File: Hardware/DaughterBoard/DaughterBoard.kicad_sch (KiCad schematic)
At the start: 19 parts, among them J1 CARTDRIGE, J10 JOYPAD2, J11 LCD, J12 POWER, J13 PA, J14 PB, J2 ROM, J3 ISA00, J4 ISA10, J7 ISA01, J8 ISA11, J9 JOYPAD1, X1 ACO-20MHz

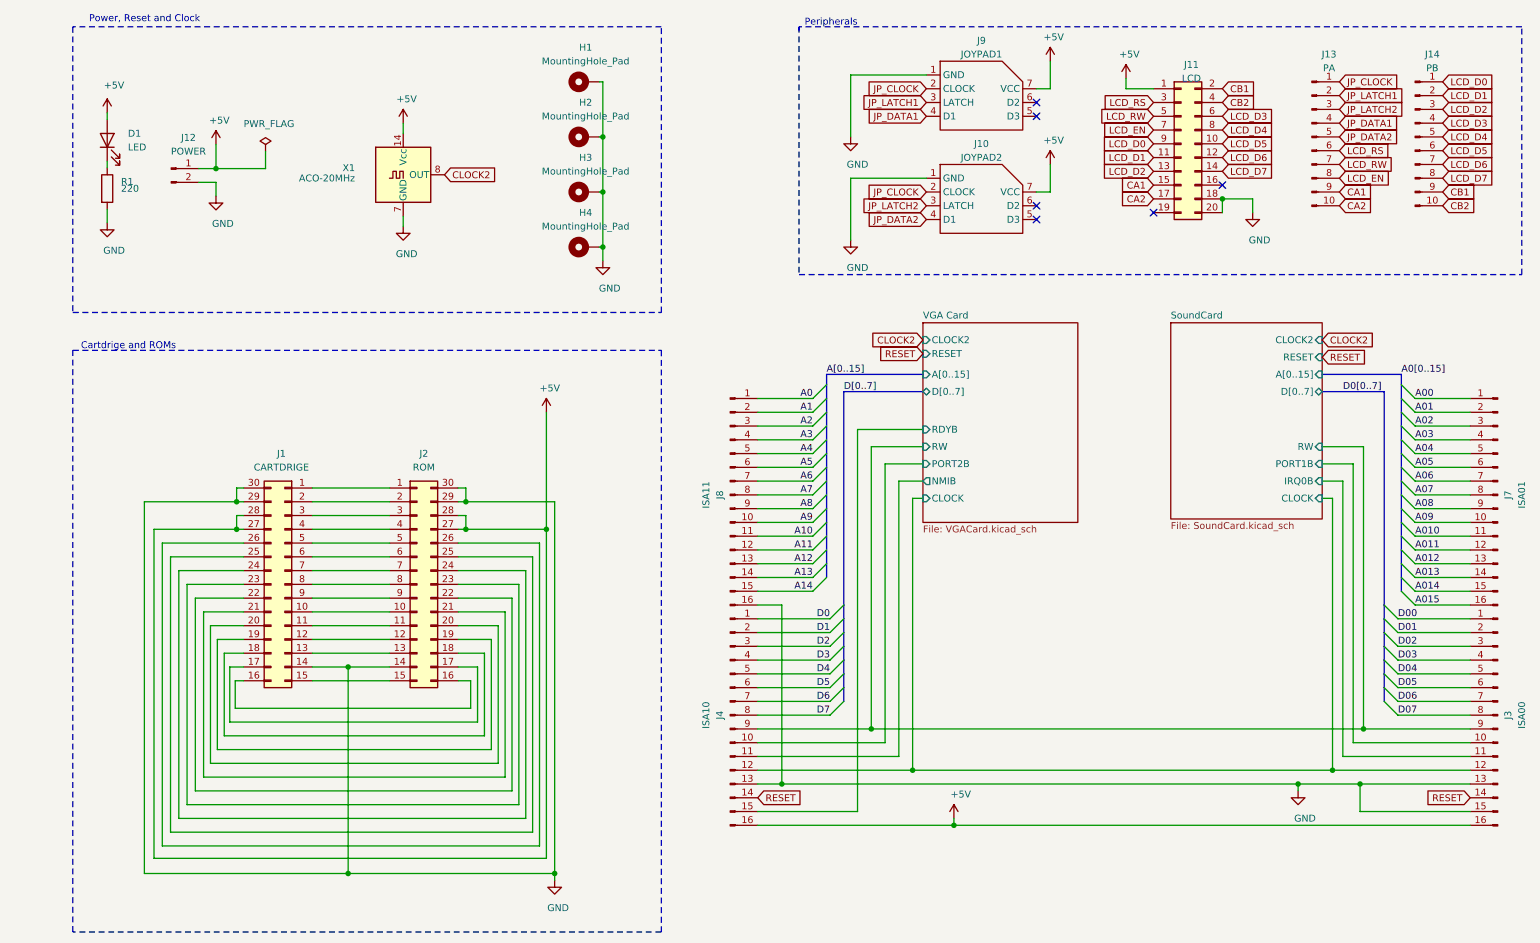
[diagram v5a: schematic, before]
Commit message: New PLD logic, VGA, DMA ...
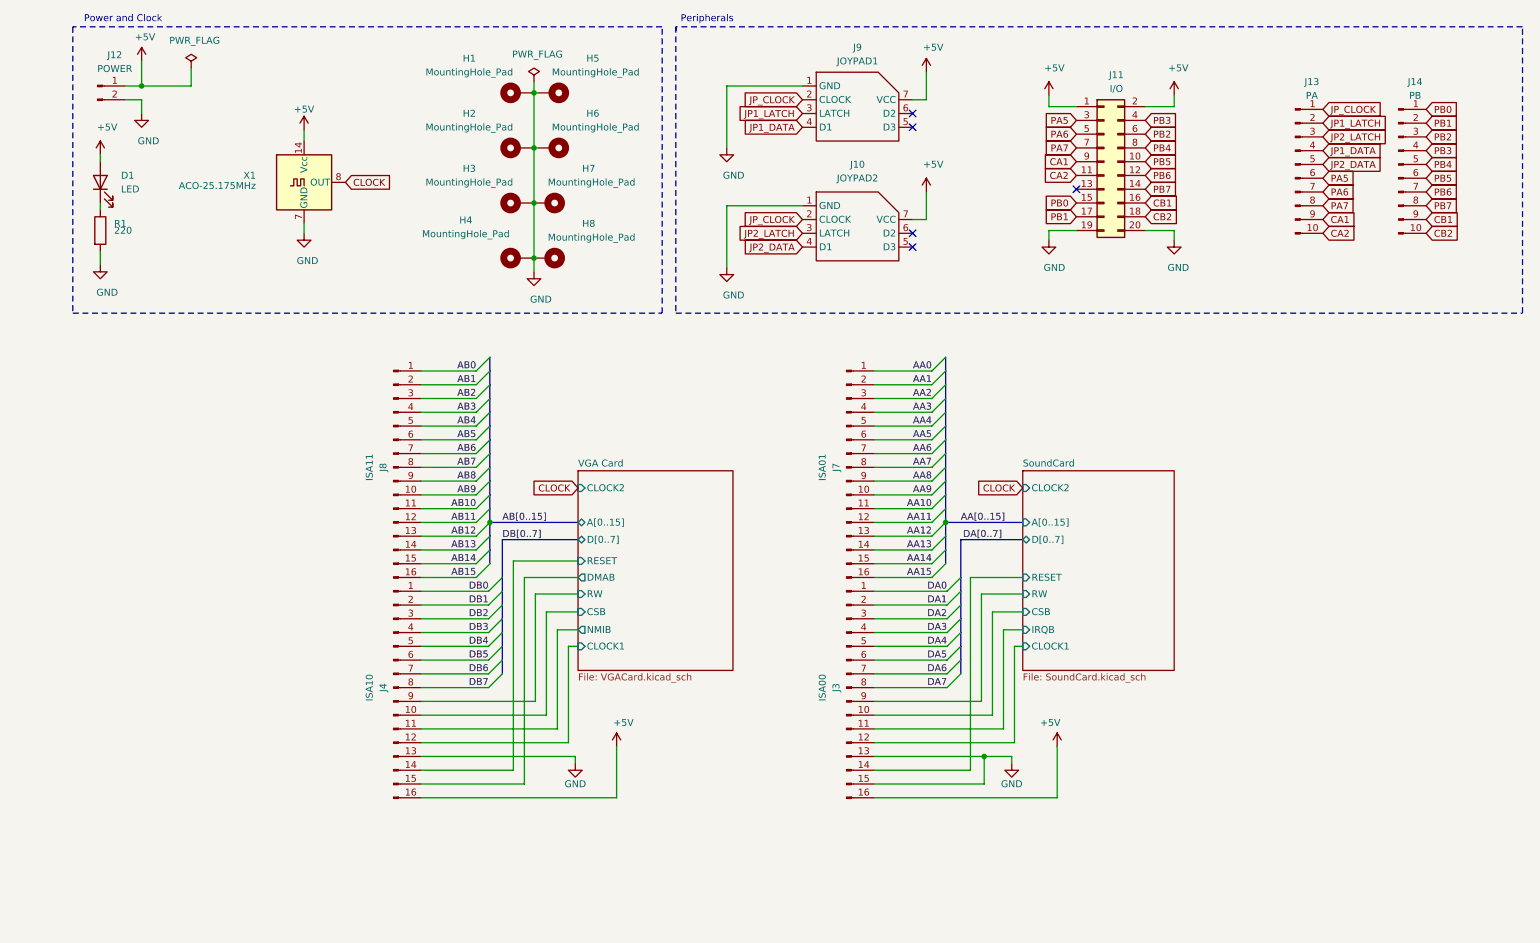
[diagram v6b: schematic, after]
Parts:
- removed J1: CARTDRIGE, Connector_PinHeader_2.54mm:PinHeader_2x15_P2.54mm_Vertical, symbol Connector_Generic:Conn_02x15_Counter_Clockwise
- removed J2: ROM, Connector_PinHeader_2.54mm:PinHeader_2x15_P2.54mm_Vertical, symbol Connector_Generic:Conn_02x15_Counter_Clockwise
- added H5, H6, H7, H8: MountingHole_Pad, MountingHole:MountingHole_3.2mm_M3, symbol Mechanical:MountingHole_Pad
- J11: value LCD -> I/O
- X1: value ACO-20MHz -> ACO-25.175MHz
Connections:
- net +5V: now also J11.2 (Pin_2)
- net CA1: now also J11.9 (Pin_9); no longer J11.15 (Pin_15)
- net CA2: now also J11.11 (Pin_11); no longer J11.17 (Pin_17)
- net CB1: now also J11.16 (Pin_16); no longer J11.2 (Pin_2)
- net CB2: now also J11.18 (Pin_18); no longer J11.4 (Pin_4)
- net GND: now also J11.19 (Pin_19), H5.1, H6.1, H7.1, H8.1; no longer J11.18 (Pin_18), J8.16 (Pin_16)
- net SoundCard/RW: no longer J4.9 (Pin_9)
- net A0 renamed AB0
- net A00 renamed AA0
- net A01 renamed AA1
- net A010 renamed AA10
- net A011 renamed AA11
- net A012 renamed AA12
- net A013 renamed AA13
- net A014 renamed AA14
- net A015 renamed AA15
- net A02 renamed AA2
- net A03 renamed AA3
- net A04 renamed AA4
- net A05 renamed AA5
- net A06 renamed AA6
- net A07 renamed AA7
- net A08 renamed AA8
- net A09 renamed AA9
- net A1 renamed AB1
- net A10 renamed AB10
- net A11 renamed AB11
- net A12 renamed AB12
- net A13 renamed AB13
- net A14 renamed AB14
- net A2 renamed AB2
- net A3 renamed AB3
- net A4 renamed AB4
- net A5 renamed AB5
- net A6 renamed AB6
- net A7 renamed AB7
- net A8 renamed AB8
- net A9 renamed AB9
- net CLOCK2 renamed CLOCK
- net D0 renamed DB0
- net D00 renamed DA0
- net D01 renamed DA1
- net D02 renamed DA2
- net D03 renamed DA3
- net D04 renamed DA4
- net D05 renamed DA5
- net D06 renamed DA6
- net D07 renamed DA7
- net D1 renamed DB1
- net D2 renamed DB2
- net D3 renamed DB3
- net D4 renamed DB4
- net D5 renamed DB5
- net D6 renamed DB6
- net D7 renamed DB7
- net JP_DATA1 renamed JP1_DATA
- net JP_DATA2 renamed JP2_DATA
- net JP_LATCH1 renamed JP1_LATCH
- net JP_LATCH2 renamed JP2_LATCH
- net LCD_D0 renamed PB0
- net PB0: now also J11.15 (Pin_15); no longer J11.9 (Pin_9)
- net LCD_D1 renamed PB1
- net PB1: now also J11.17 (Pin_17); no longer J11.11 (Pin_11)
- net LCD_D2: no longer names the net of J11.13 (Pin_13)
- net LCD_D2: no longer J14.3 (Pin_3)
- net LCD_D3 renamed PB2
- net PB2: now also J14.3 (Pin_3); no longer J14.4 (Pin_4)
- net LCD_D4 renamed PB4
- net LCD_D5 renamed PB5
- net LCD_D6 renamed PB6
- net LCD_D7 renamed PB7
- net LCD_EN renamed PA7
- net LCD_RS renamed PA5
- net LCD_RW renamed PA6
- net RESET renamed SoundCard/RESET
- net SoundCard/RESET: no longer J4.14 (Pin_14)
- net SoundCard/CLOCK renamed SoundCard/CLOCK1
- net SoundCard/CLOCK1: no longer J4.12 (Pin_12)
- net SoundCard/IRQ0B renamed SoundCard/IRQB
- net SoundCard/PORT1B renamed SoundCard/CSB
- net VGA Card/PORT2B renamed VGA Card/CSB
- net VGA Card/RDYB renamed VGA Card/DMAB
- new net AB15: J8.16 (Pin_16)
- new net PB3: J11.4 (Pin_4), J14.4 (Pin_4)
- new net VGA Card/CLOCK1: J4.12 (Pin_12)
- new net VGA Card/RESET: J4.14 (Pin_14)
- new net VGA Card/RW: J4.9 (Pin_9)
- no-connect marks 6 -> 5
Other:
- sheet SoundCard ports: added CLOCK1, CSB, IRQB; removed CLOCK, IRQ0B, PORT1B
- sheet VGA Card ports: added CLOCK1, CSB, DMAB; removed CLOCK, PORT2B, RDYB
- note added: "Power and Clock"
- note removed: "Cartdrige and ROMs"
- note removed: "Power, Reset and Clock"
- moved on the sheet: D1, H1, H2, H3, H4, J10, J11, J12, J13, J14, J3, J4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

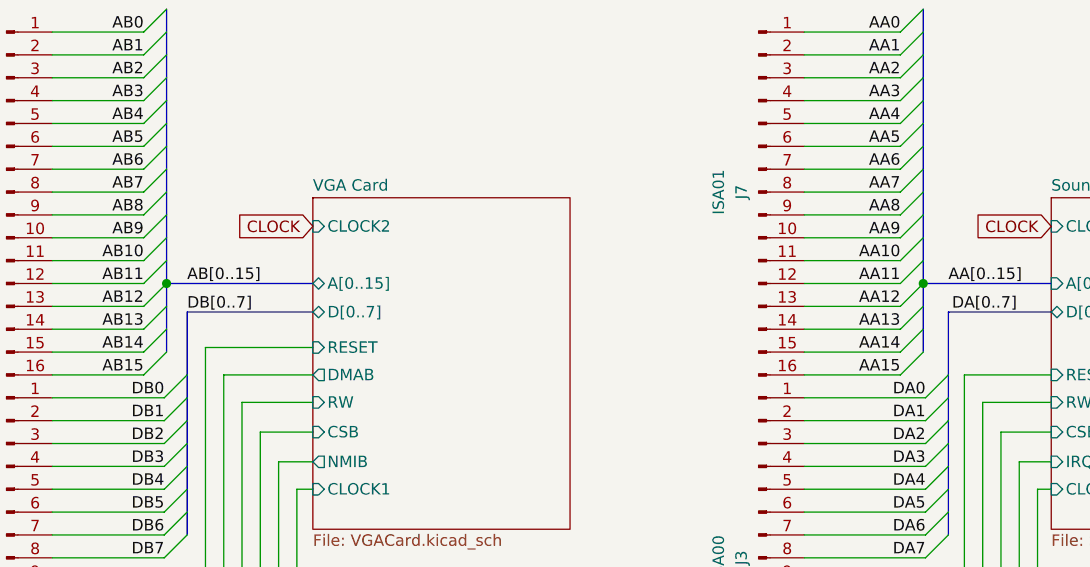
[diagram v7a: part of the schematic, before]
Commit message: Update to Kicad 6.0
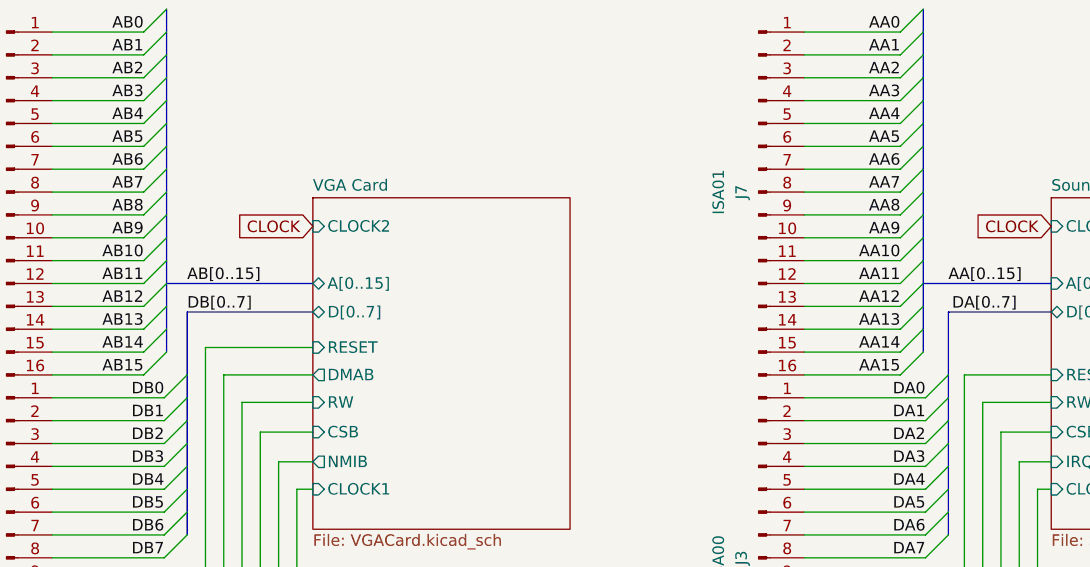
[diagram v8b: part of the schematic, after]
